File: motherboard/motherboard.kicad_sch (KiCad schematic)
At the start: 24 parts, among them J1 USART6, J14 USB_C_Receptacle_USB2.0, J2 USART1, J4 SPI2, J5 SPI1, SW1 MCU_RST, U2 AZ1117-3.3, U2 STM32F412RETx, Y1 8M

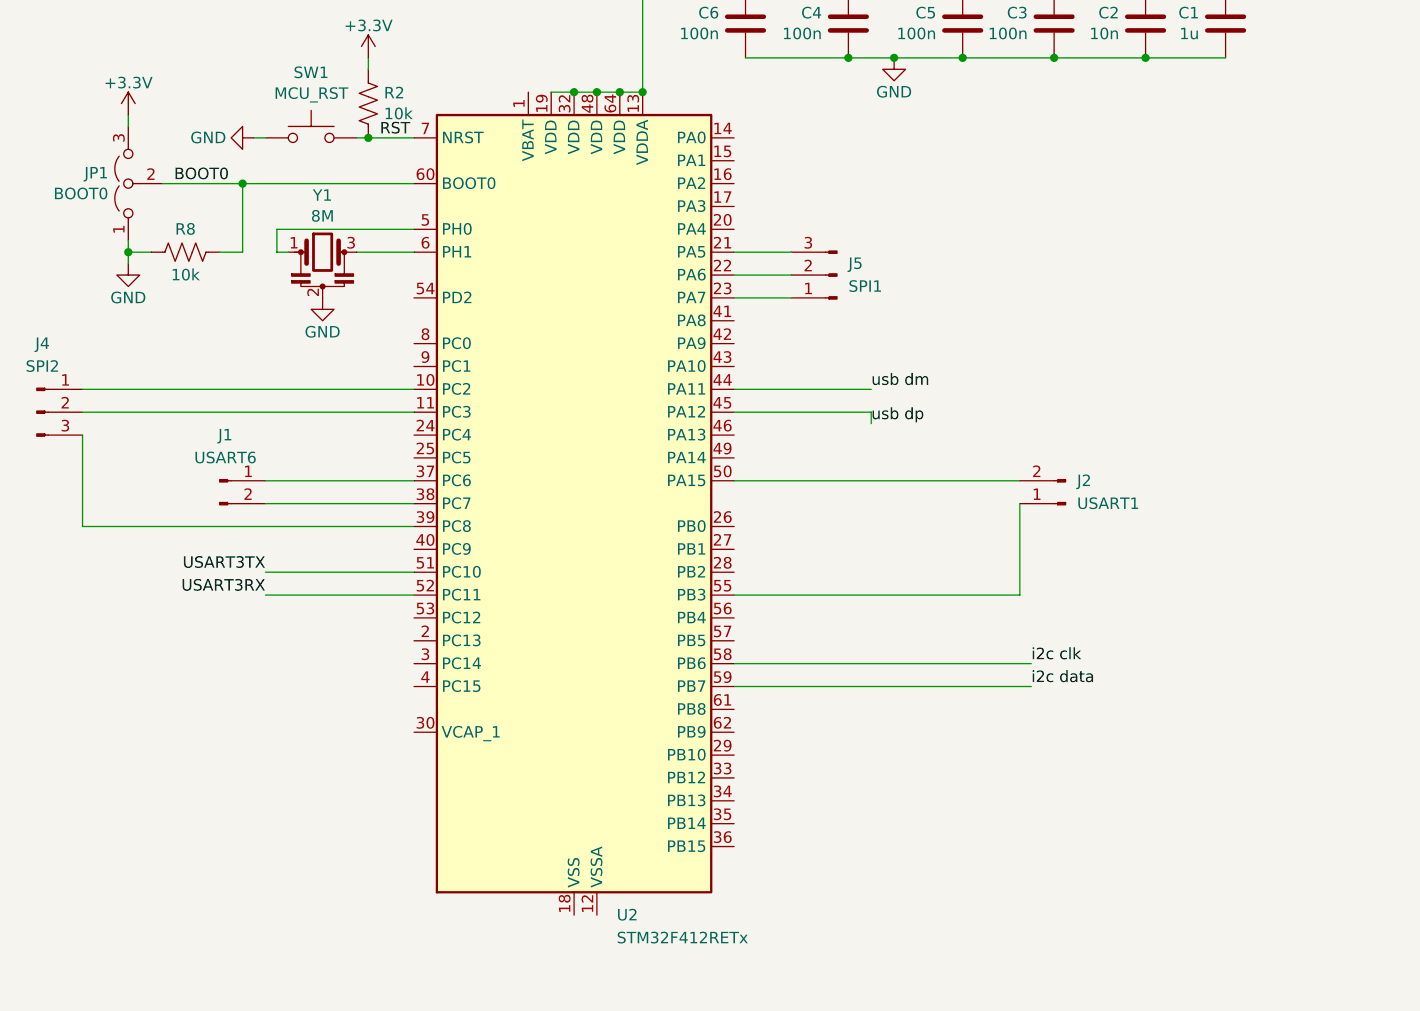
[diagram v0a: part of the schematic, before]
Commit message: Add new connections
Added UART and SPI Pin connections
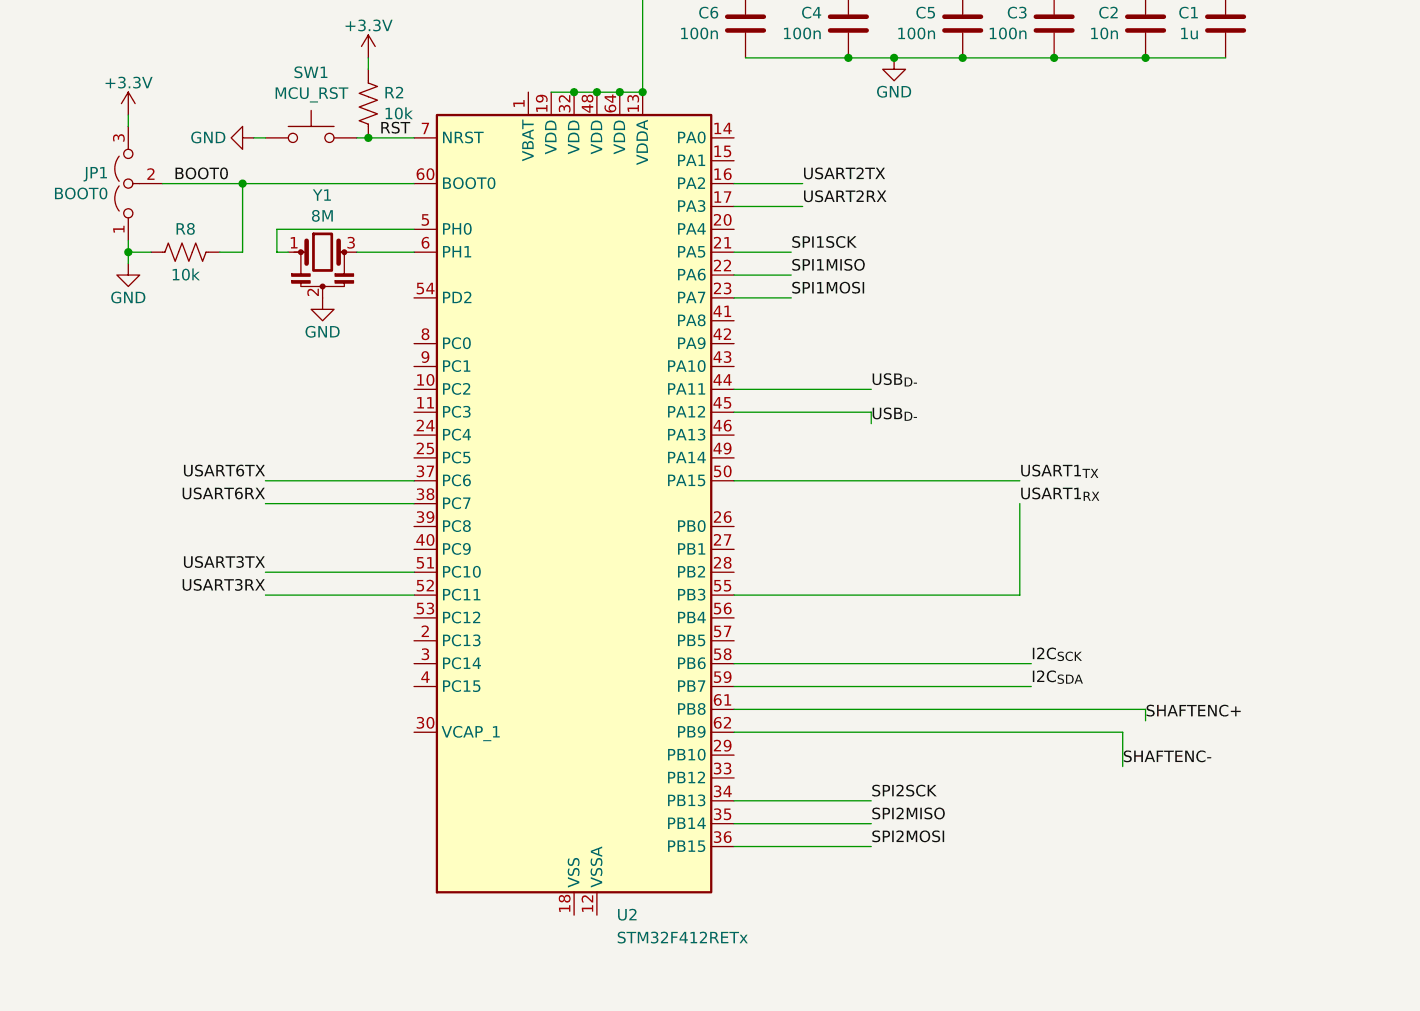
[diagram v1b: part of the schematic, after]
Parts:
- removed J1: USART6, symbol Connector:Conn_01x02_Pin
- removed J2: USART1, symbol Connector:Conn_01x02_Pin
- removed J4: SPI2, symbol Connector:Conn_01x03_Pin
- removed J5: SPI1, symbol Connector:Conn_01x03_Pin
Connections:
- net usb dp is gone; now on net USB_{D-}: U2.45 (PA12)
- net USART6TX: now reaches U2.37 (PC6)
- net USART6RX: now reaches U2.38 (PC7)
- net SPI1MOSI: now reaches U2.23 (PA7)
- net SPI1MISO: now reaches U2.22 (PA6)
- net SPI1SCK: now reaches U2.21 (PA5)
- net USART1_{RX}: now reaches U2.55 (PB3)
- net USART1_{TX}: now reaches U2.50 (PA15)
- net USART2TX: now reaches U2.16 (PA2)
- net USART2RX: now reaches U2.17 (PA3)
- net SPI2SCK: now reaches U2.34 (PB13)
- net SPI2MISO: now reaches U2.35 (PB14)
- net SPI2MOSI: now reaches U2.36 (PB15)
- net SHAFTENC+: now reaches U2.61 (PB8)
- net SHAFTENC-: now reaches U2.62 (PB9)
- net i2c clk renamed I2C_{SCK}
- net i2c data renamed I2C_{SDA}
- net usb dm renamed USB_{D-}

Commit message: Motherboard I/O streams
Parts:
- added J1: Raspberry_Pi_2_3, symbol Connector:Raspberry_Pi_2_3
- added J10: orientation, symbol Connector:Conn_01x02_Pin
- added J11: shaft enc, symbol Connector:Conn_01x02_Pin
- added J12: coding, symbol Connector:Conn_01x02_Pin
- added J13: barometer, symbol Connector:Conn_01x02_Pin
- added J14: spar load, symbol Connector:Conn_01x01_Pin
- added J15: Lidar, symbol Connector:Conn_01x02_Pin
- added J2: Telemetry Mod., symbol Connector:Conn_01x03_Pin
- added J3: 6 axis IMU, symbol Connector:Conn_01x03_Pin
- added J4: Bluetooth module, symbol Connector:Conn_01x02_Pin
- added J5: GPS, symbol Connector:Conn_01x02_Pin
- added J7: Control System, symbol Connector:Conn_01x02_Pin
- added J8: power Monitor, symbol Connector:Conn_01x02_Pin
- added J9: Pitot-Static, symbol Connector:Conn_01x02_Pin
- added U3: DPS310, Package_LGA:Bosch_LGA-8_2x2.5mm_P0.65mm_ClockwisePinNumbering, symbol mb_sensors:DPS310
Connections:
- net USB- is gone; now on net USB_{D-}: R10.1
- net +3.3V: now also J1.1 (3V3), J1.17 (3V3), U3.6 (V_{DDIO}), U3.8 (V_{DD})
- net +5V: now also J1.2 (5V), J1.4 (5V)
- net GND: now also J1.14 (GND), J1.20 (GND), J1.25 (GND), J1.30 (GND), J1.34 (GND), J1.39 (GND), J1.6 (GND), J1.9 (GND), U3.1 (GND), U3.7 (GND)
- net I2C_{SCK}: now also J10.2 (Pin_2), J11.2 (Pin_2), J13.2 (Pin_2), J15.2 (Pin_2), J7.2 (Pin_2), J8.2 (Pin_2), J9.2 (Pin_2), U3.4 (SCK)
- net I2C_{SDA}: now also J10.1 (Pin_1), J11.1 (Pin_1), J13.1 (Pin_1), J15.1 (Pin_1), J7.1 (Pin_1), J8.1 (Pin_1), J9.1 (Pin_1), U3.3 (SDI)
- net SPI1MISO: now also J2.2 (Pin_2)
- net SPI1MOSI: now also J2.1 (Pin_1)
- net SPI1SCK: now also J2.3 (Pin_3)
- net SPI2MISO: now also J3.2 (Pin_2)
- net SPI2MOSI: now also J3.1 (Pin_1)
- net SPI2SCK: now also J3.3 (Pin_3)
- net USART1_{RX}: now also J5.1 (Pin_1)
- net USART1_{TX}: now also J5.2 (Pin_2)
- net USART3RX: now also J1.10 (GPIO15/RXD)
- net USART3TX: now also J1.8 (GPIO14/TXD)
- net USART6RX: now also J4.1 (Pin_1)
- net USART6TX: now also J4.2 (Pin_2)
- net USB_{D-}: now also J12.1 (Pin_1); no longer U2.44 (PA11)
- net spar load: now reaches U2.11 (PC3)
- net spar load: now also J14.1 (Pin_1)
- net USB+ renamed USB_{D+}
- net USB_{D+}: now also U2.44 (PA11), J12.2 (Pin_2)
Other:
- moved on the sheet: C1, C2, C3, C4, C5, C6, C7, C8, J14, JP1, R10, R11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

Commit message: insertion of imu, gps, telemetery, etc.
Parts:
- removed J2: Telemetry Mod., symbol Connector:Conn_01x03_Pin
- removed J3: 6 axis IMU, symbol Connector:Conn_01x03_Pin
- removed J4: Bluetooth module, symbol Connector:Conn_01x02_Pin
- added C9: 10nf, symbol Device:C
- added IMU6axis: ~, symbol mb_sensors:ICM-42688-P
- added J2: Blutooth Module, symbol Connector:Conn_01x06_Pin
- added U4: ~, symbol mb_MT3339:MT3339
- added U5: telemetry, RF_Module:nRF24L01_Breakout, symbol RF:NRF24L01_Breakout
- added U6: DHT11, Sensor:Aosong_DHT11_5.5x12.0_P2.54mm, symbol Sensor:DHT11
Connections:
- net +3.3V: now also C9.1, IMU6axis.5 (vddio), U4.1 (3.3V), U4.8 (VIN), U5.2 (VCC)
- net +5V: now also J2.5 (Pin_5)
- net GND: now also C9.2, IMU6axis.11 (resv), IMU6axis.6 (gnd), IMU6axis.7 (resv), J2.4 (Pin_4), U4.7 (GND), U5.1 (GND)
- net SPI1MISO: now also U5.7 (MISO)
- net SPI1MOSI: now also U5.6 (MOSI)
- net SPI1SCK: now also U5.5 (SCK)
- net SPI2MISO: now also IMU6axis.1 (SDO)
- net SPI2MOSI: now also IMU6axis.14 (SDI)
- net SPI2SCK: now also IMU6axis.13 (SCK)
- net USART1_{RX}: now also U4.6 (RX)
- net USART1_{TX}: now also U4.5 (TX)
- net USART6RX: now also J2.2 (Pin_2)
- net USART6TX: now also J2.3 (Pin_3)
- new net IMU_cs: IMU6axis.12 (CS), IMU6axis.4 (INT)
- new net tele_ce: U5.3 (CE)
- new net tele_cs: U5.4 (~{CSN})
- new net tele_irq: U5.8 (IRQ)
- no-connect marks 3 -> 9
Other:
- moved on the sheet: C1, C2, C3, C4, C5, C6, C7, C8, J14, R10, R11, R12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

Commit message: Adding Components to motherboard
Added HC-05 and MH-Z19 To the motherboard schematic
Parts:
- added U7: ~, symbol mb_sensors:HC-05
- U3: value DPS310 -> DPS310 - barometer
- U5: value telemetry -> nRF24L01-telemetry
- U6: value DHT11 -> DHT11(DHT22)
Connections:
- net +3.3V: now also U7.2 (VCC)
- net GND: now also U7.3 (GND)
- net USART6RX: now also U7.4 (TX)
- net USART6TX: now also U7.5 (RX)
- no-connect marks 9 -> 10
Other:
- moved on the sheet: J1, J14, J2

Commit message: Completed First Draft of Motherboard Schematic
Added in second bluetooth module, corrected pin allocations, fixed schematic symbols
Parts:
- removed J13: barometer, symbol Connector:Conn_01x02_Pin
- removed J2: Blutooth Module, symbol Connector:Conn_01x06_Pin
- removed J5: GPS, symbol Connector:Conn_01x02_Pin
- added U8: Bluetooth Module - Power Controller, symbol mb_sensors:HC-05
- J1: value Raspberry_Pi_2_3 -> Raspberry_Pi_2_3 ANT
- J10: value orientation -> Orientation Sensor
- J7: value Control System -> Control Board
- J8: value power Monitor -> Battery Monitor
- U4: value ~ -> GPS module
- U7: value ~ -> Bluetooth Module - Shaft Power
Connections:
- net +3.3V: now also U8.2 (VCC)
- net GND: now also U8.3 (GND)
- net I2C_{SCK}: no longer J11.2 (Pin_2)
- net I2C_{SDA}: no longer J11.1 (Pin_1)
- net SHAFTENC+: now also J11.2 (Pin_2)
- net SHAFTENC-: now also J11.1 (Pin_1)
- net USART2RX renamed USART2_{RX}
- net USART2_{RX}: now also U8.4 (TX)
- net USART2TX renamed USART2_{TX}
- net USART2_{TX}: now also U8.5 (RX)
- net spar load renamed SparLoad
- no-connect marks 10 -> 8
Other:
- moved on the sheet: C1, C2, C3, C4, C5, C6, C7, C8, C9, IMU6axis, J10, J11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

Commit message: Edited Headers added power and ground pins to external board headers, added ground to MC, added capictor to I2C
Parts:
- removed J10: Orientation Sensor, symbol Connector:Conn_01x02_Pin
- removed J11: shaft enc, symbol Connector:Conn_01x02_Pin
- removed J15: Lidar, symbol Connector:Conn_01x02_Pin
- removed J7: Control Board, symbol Connector:Conn_01x02_Pin
- removed J8: Battery Monitor, symbol Connector:Conn_01x02_Pin
- removed J9: Pitot-Static, symbol Connector:Conn_01x02_Pin
- added C10: 4.7u, symbol Device:C
- added J11: Control Board, symbol Connector:Conn_01x05_Pin
- added J2: shaftencorder, symbol Connector:Conn_01x03_Pin
- added J3: c02 censor, symbol Connector:Conn_01x03_Pin
- added J4: Battery / Pitot/ Orientation, symbol Connector:Conn_01x04_Pin
- added J5: lidar, symbol Connector:Conn_01x04_Pin
- added R8: 100k, symbol Device:R_US
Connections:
- net +3.3V: now also U6.1 (VCC), J11.2 (Pin_2), J2.3 (Pin_3), J4.2 (Pin_2)
- net +5V: now also J11.3 (Pin_3), J3.3 (Pin_3), J5.4 (Pin_4)
- net GND: now also U2.12 (VSSA), U2.18 (VSS), U2.31 (VSS), U2.47 (VSS), U2.63 (VSS), U6.4 (GND), C10.2, J11.1 (Pin_1), J2.1 (Pin_1), J3.1 (Pin_1), J4.1 (Pin_1), J5.1 (Pin_1), R8.1
- net I2C_{SCK}: now also J11.5 (Pin_5), J4.4 (Pin_4), J5.3 (Pin_3)
- net I2C_{SDA}: now also J11.4 (Pin_4), J4.3 (Pin_3), J5.2 (Pin_2)
- net IMU_cs: now also U2.29 (PB10)
- net C_{O2}: now reaches U2.26 (PB0)
- net C_{O2}: now also J3.2 (Pin_2)
- net DHT22: now reaches U2.27 (PB1)
- net DHT22: now also U6.2 (IO)
- net at U2.30 (VCAP_1): now also C10.1, R8.2
- net SHAFTENC+ renamed SHAFTENC
- net SHAFTENC: now also J2.2 (Pin_2)
- net SHAFTENC-: no longer names the net of U2.62 (PB9)
- no-connect marks 8 -> 10
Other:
- moved on the sheet: U7, U8

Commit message: Added power to output headers
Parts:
- removed J14: spar load, symbol Connector:Conn_01x01_Pin
- added J7: SparLoad, symbol Connector:Conn_01x03_Pin
- added R7: 100k, symbol Device:R_US
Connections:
- net +3.3V: now also IMU6axis.8 (VDD)
- net +5V: now also J7.1 (Pin_1)
- net DHT22: now also R7.2
- net GND: now also J7.3 (Pin_3), R7.1
- net SparLoad: now also J7.2 (Pin_2)
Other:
- moved on the sheet: J3

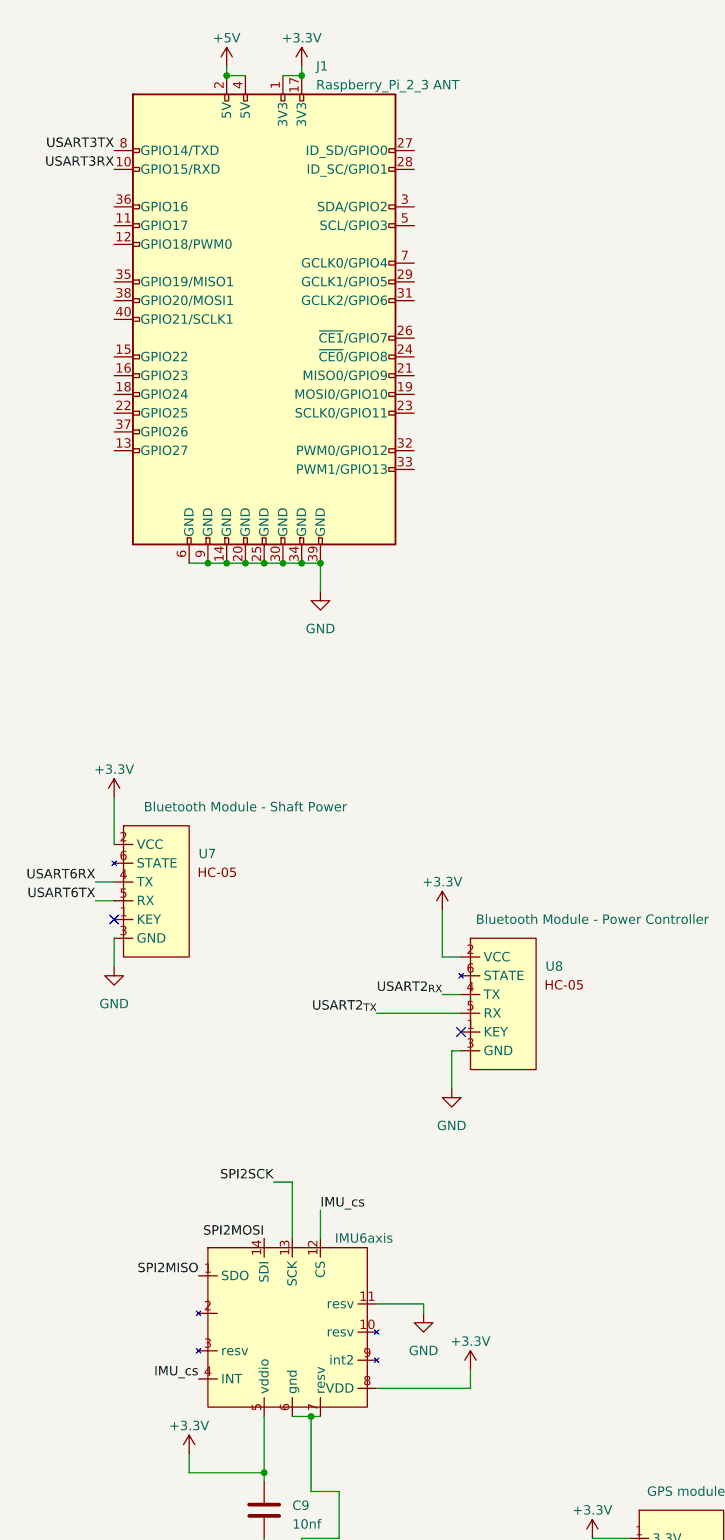
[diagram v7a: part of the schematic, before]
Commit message: Fixed up some schmatic symbols
Fixed schematic symbols for hc-05 and the 6 axis IMU
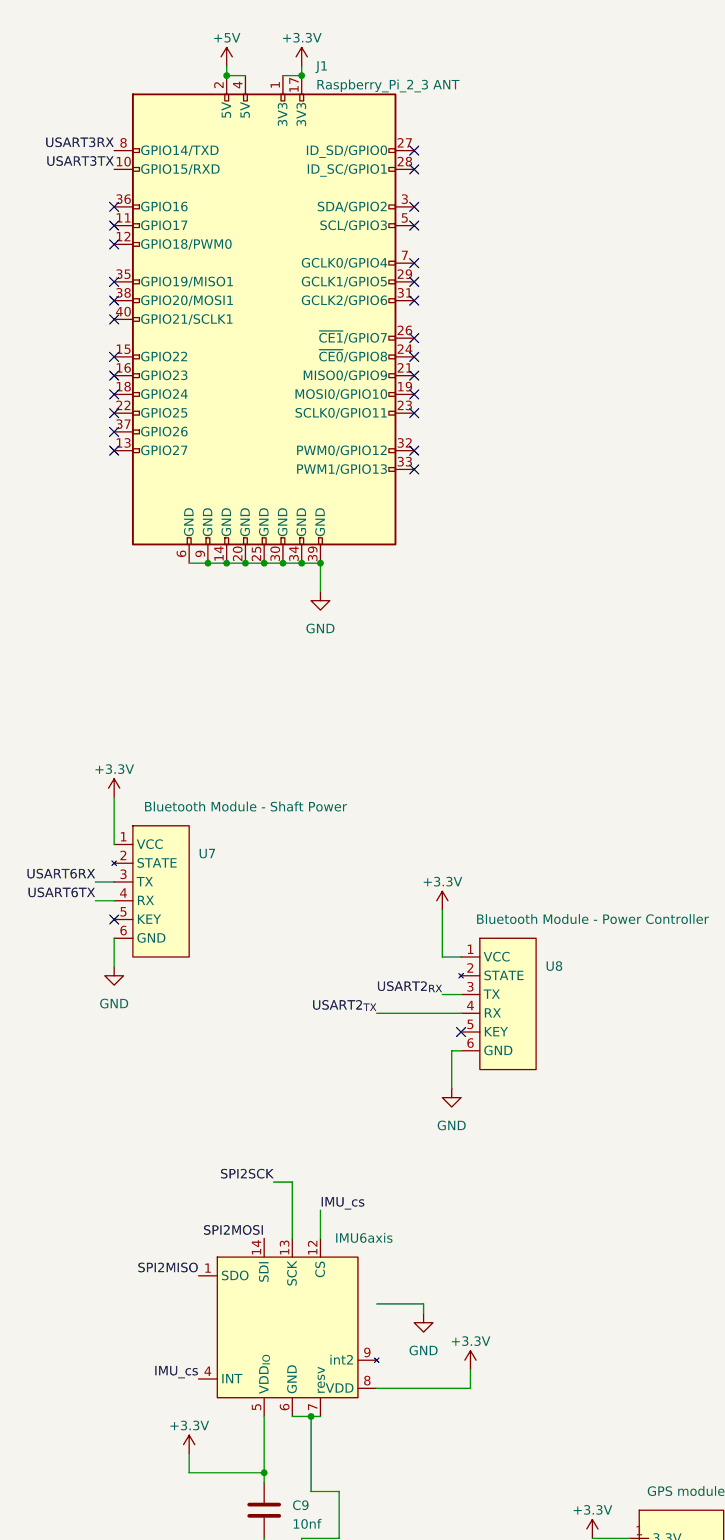
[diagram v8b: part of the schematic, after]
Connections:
- net +3.3V: now also U7.1 (VCC), U8.1 (VCC); no longer U7.2 (VCC), U8.2 (VCC)
- net GND: now also U7.6 (GND), U8.6 (GND); no longer U7.3 (GND), U8.3 (GND)
- net USART2_{RX}: now also U8.3 (TX); no longer U8.4 (TX)
- net USART2_{TX}: now also U8.4 (RX); no longer U8.5 (RX)
- net USART3RX: now also J1.8 (GPIO14/TXD); no longer J1.10 (GPIO15/RXD)
- net USART3TX: now also J1.10 (GPIO15/RXD); no longer J1.8 (GPIO14/TXD)
- net USART6RX: now also U7.3 (TX); no longer U7.4 (TX)
- net USART6TX: now also U7.4 (RX); no longer U7.5 (RX)
- net at IMU6axis.2 (resv): now also IMU6axis.3 (resv)
- no-connect marks 10 -> 36
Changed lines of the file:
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@@
   (junction (at 219.71 156.21) (diameter 0) (color 0 0 0 0)
   )
+  (no_connect (at 38.1 83.82))
   (no_connect (at 38.1 147.32))
+  (no_connect (at 38.1 60.96))
   (no_connect (at 403.86 69.85))
+  (no_connect (at 78.74 58.42))
   (no_connect (at 381 59.69))
+  (no_connect (at 78.74 63.5))
+  (no_connect (at 38.1 50.8))
+  (no_connect (at 78.74 73.66))
+  (no_connect (at 38.1 76.2))
+  (no_connect (at 38.1 63.5))
+  (no_connect (at 78.74 43.18))
+  (no_connect (at 38.1 71.12))
+  (no_connect (at 38.1 55.88))
   (no_connect (at 85.09 162.56))
+  (no_connect (at 78.74 76.2))
+  (no_connect (at 38.1 66.04))
+  (no_connect (at 78.74 60.96))
+  (no_connect (at 78.74 83.82))
+  (no_connect (at 78.74 45.72))
   (no_connect (at 381 62.23))
+  (no_connect (at 38.1 81.28))
+  (no_connect (at 38.1 53.34))
+  (no_connect (at 78.74 53.34))
+  (no_connect (at 38.1 78.74))
+  (no_connect (at 78.74 78.74))
+  (no_connect (at 38.1 73.66))
   (no_connect (at 377.19 207.01))
   (no_connect (at 397.51 210.82))
+  (no_connect (at 78.74 50.8))
+  (no_connect (at 78.74 86.36))
+  (no_connect (at 78.74 68.58))
   (no_connect (at 107.95 238.76))
   (no_connect (at 107.95 236.22))
   (no_connect (at 107.95 251.46))
+  (no_connect (at 78.74 71.12))
   (wire (pts (xy 234.95 77.47) (xy 242.57 77.47))
     (stroke (width 0) (type default))
@@
     (effects (font (size 1.27 1.27)) (justify right bottom))
   )
-  (label "USART3RX" (at 38.1 45.72 180) (fields_autoplaced)
+  (label "USART3RX" (at 38.1 43.18 180) (fields_autoplaced)
     (effects (font (size 1.27 1.27)) (justify right bottom))
   )
@@
     (effects (font (size 1.27 1.27)) (justify right bottom))
   )
-  (label "USART3TX" (at 38.1 43.18 180) (fields_autoplaced)
-    (effects (font (size 1.27 1.27)) (justify right bottom))
-  )
   (label "SPI2MOSI" (at 237.49 148.59 0) (fields_autoplaced)
     (effects (font (size 1.27 1.27)) (justify left bottom))
@@
     (effects (font (size 1.27 1.27)) (justify right bottom))
   )
+  (label "USART3TX" (at 38.1 45.72 180) (fields_autoplaced)
+    (effects (font (size 1.27 1.27)) (justify right bottom))
+  )
